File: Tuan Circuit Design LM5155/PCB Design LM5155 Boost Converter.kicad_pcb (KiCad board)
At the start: 4 copper layers, 80.2 x 53 mm, 40 parts, among them Q1 BSC035N04LS G, U1 LM5155_DSSR

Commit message: Fix Update
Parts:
- moved C4 2.06 mm to (131.4, 71.8)
- moved C3 1.27 mm to (130.7, 79.9)
- renumbered Vin1 to VIN, Vout1 to VOUT
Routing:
- net /MOSFET: track 46.0 -> 46.9 mm
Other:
- board size 80.2 x 53 mm -> 80 x 53 mm

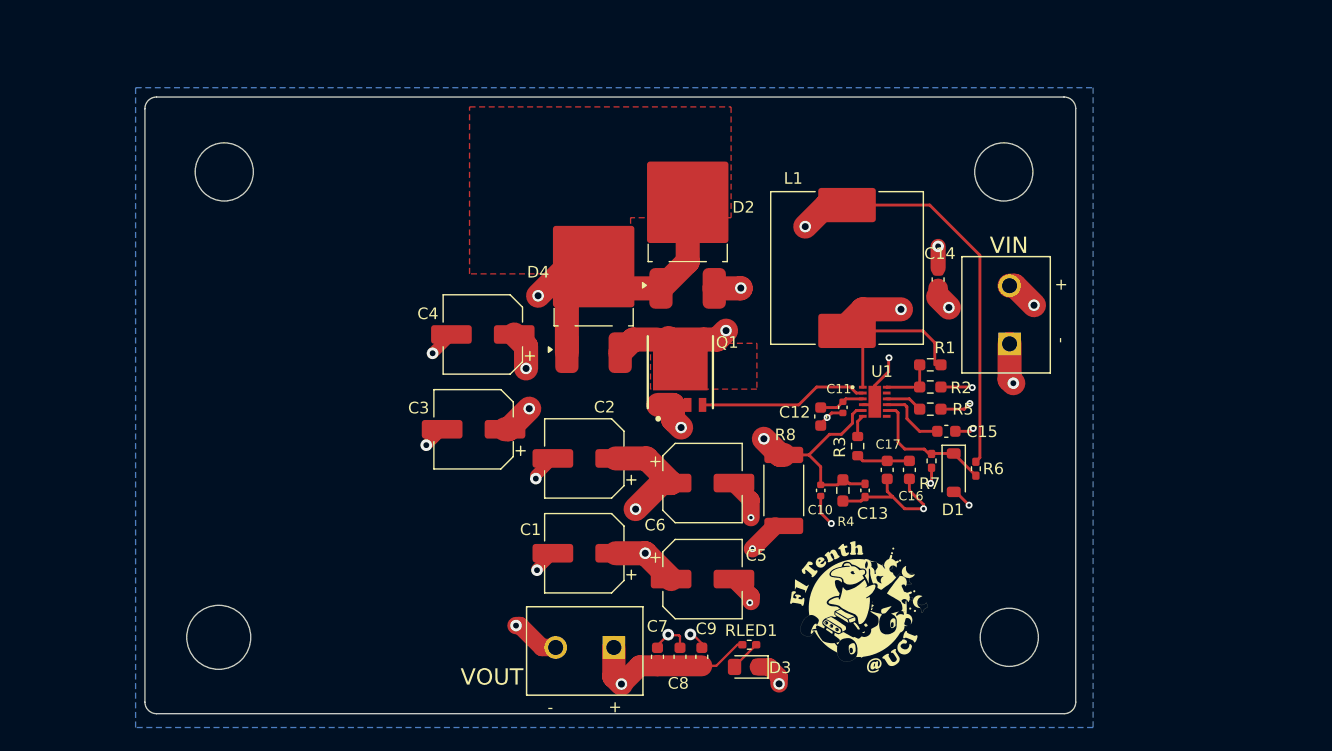
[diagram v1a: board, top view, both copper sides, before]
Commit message: Fix small issue on connection and add resistor
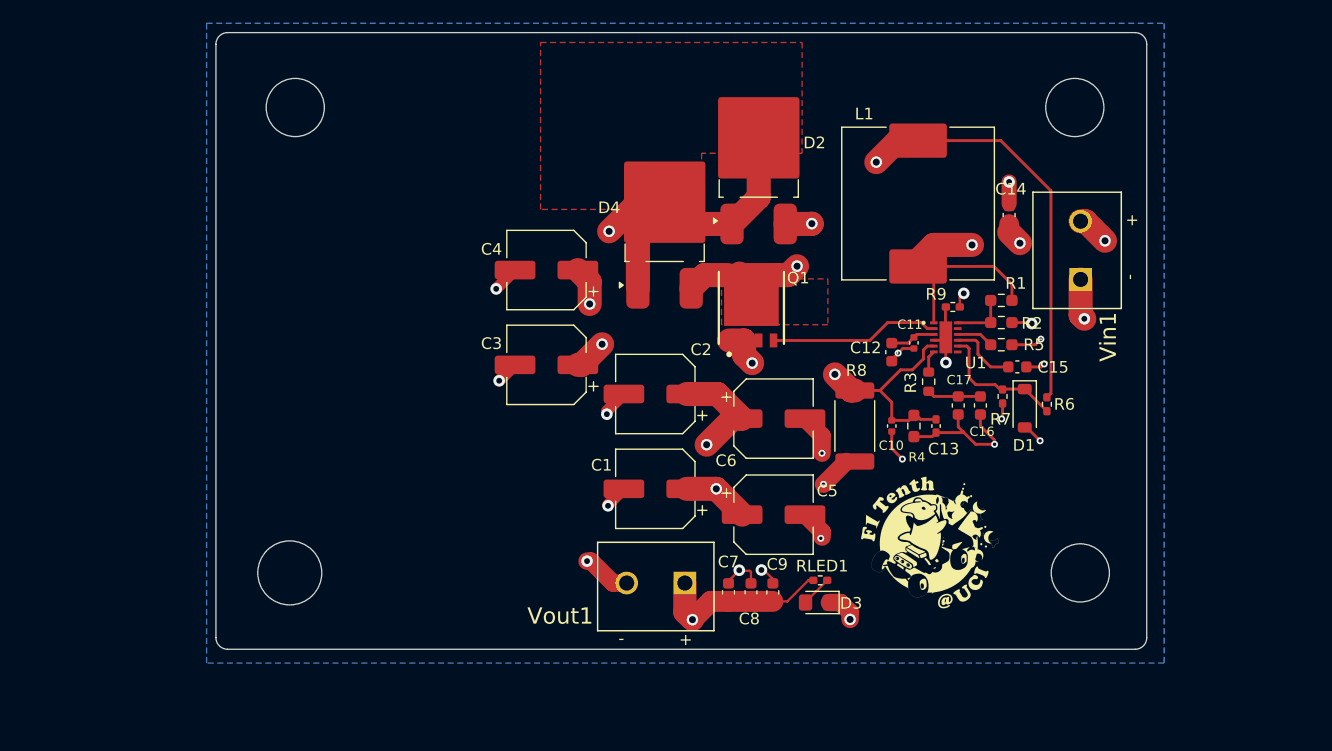
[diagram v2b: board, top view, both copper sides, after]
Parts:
- removed the REF** at (176.7, 97.8)
- removed the REF** at (176.2, 57.8)
- removed the REF** at (109.2, 57.8)
- removed VIN, VOUT: TB002-500-02BE, TB002_500_02BE:CUI_TB002-500-02BE
- added R9: 0, Resistor_SMD:R_0402_1005Metric_Pad0.72x0.64mm_HandSolder, F.Cu at (171.8, 69.4)
- added REF**: MountingHole_5mm, MountingHole:MountingHole_5mm, F.Cu at (182.8, 92.2)
- added REF**: MountingHole_5mm, MountingHole:MountingHole_5mm, F.Cu at (182.3, 52.2)
- added REF**: MountingHole_5mm, MountingHole:MountingHole_5mm, F.Cu at (115.3, 52.2)
- added Vin1: TB002-500-02BE, TB002_500_02BE:CUI_TB002-500-02BE, F.Cu at (182.8, 67.0)
- added Vout1: TB002-500-02BE, TB002_500_02BE:CUI_TB002-500-02BE, F.Cu at (148.8, 93.1)
- moved C3 8.36 mm to (136.9, 74.4)
- moved C12 8.24 mm to (166.6, 73.3)
- moved Q1 8.24 mm to (154.5, 69.5)
- moved U1 8.24 mm to (171.2, 72.0)
- moved C14 8.24 mm to (176.7, 61.5)
- moved D2 8.24 mm to (155.2, 56.9)
- moved C10 8.24 mm to (166.6, 79.6)
- moved C11 8.24 mm to (168.5, 72.5)
- moved C13 8.24 mm to (170.4, 79.6)
- moved C15 8.24 mm to (177.4, 74.5)
- moved C7 8.24 mm to (152.6, 93.9)
- moved C8 8.24 mm to (154.5, 93.9)
- moved C9 8.24 mm to (156.4, 93.9)
- moved D4 8.24 mm to (147.1, 62.4)
- moved R4 8.24 mm to (168.5, 79.6)
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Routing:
- net GNDPWR: track 43.8 -> 44.3 mm
- net GND: track 24.9 -> 25.3 mm, vias 7 -> 8

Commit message: Add switch
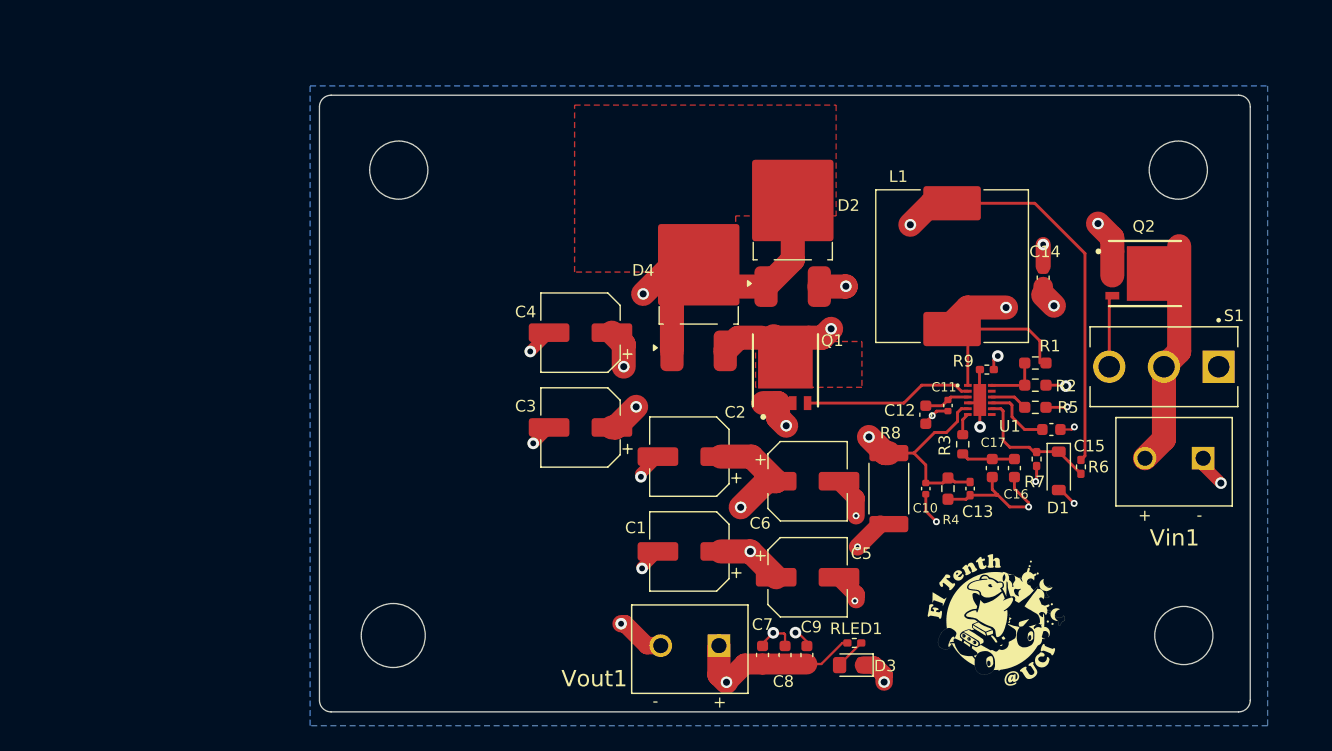
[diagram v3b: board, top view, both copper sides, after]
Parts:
- removed the REF** at (182.8, 92.2)
- removed the REF** at (182.3, 52.2)
- removed the REF** at (115.3, 52.2)
- added Q2: BSC035N04LS G, INF-PG-TDSON-8:INF-PG-TDSON-8, F.Cu at (188.4, 66.5)
- added REF**: MountingHole_5mm, MountingHole:MountingHole_5mm, F.Cu at (124.2, 57.6)
- added REF**: MountingHole_5mm, MountingHole:MountingHole_5mm, F.Cu at (191.2, 57.6)
- added REF**: MountingHole_5mm, MountingHole:MountingHole_5mm, F.Cu at (191.7, 97.6)
- added S1: 100SP1T1B4M2QE, SW_100SP1T1B4M2QE:SW_100SP1T1B4M2QE, F.Cu at (190.0, 74.5)
- moved Vin1 18.6 mm to (193.4, 82.4), turned to 180 degrees
- moved REF** 10.4 mm to (123.7, 97.6)
- moved Ref 8.77 mm to (176.3, 96.4)
- moved C1 6.13 mm to (149.2, 90.4)
- moved C16 6.13 mm to (177.1, 83.2)
- moved C17 6.13 mm to (175.2, 83.2)
- moved C2 6.13 mm to (149.2, 82.3)
- moved C3 6.13 mm to (139.8, 79.7)
- moved C4 6.13 mm to (139.8, 71.6)
- moved C5 6.13 mm to (159.4, 92.6)
- moved C6 6.13 mm to (159.4, 84.4)
- moved D1 6.13 mm to (180.9, 83.5)
- moved D3 6.13 mm to (163.1, 100.2)
- moved R1 6.13 mm to (178.9, 74.2)
- moved R2 6.13 mm to (178.9, 76.1)
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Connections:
- Vin1 pad 2: /INDUCTOR -> Net-(Q2-DRAIN-Pad5)
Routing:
- net Net-(Q2-DRAIN-Pad5): track 0.00 -> 19.4 mm
- net Net-(Q2-GATE): track 0.00 -> 6.21 mm
- net /INDUCTOR: track 26.0 -> 28.0 mm
- net GND: track 25.3 -> 24.1 mm
- net GNDPWR: track 44.3 -> 43.8 mm

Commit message: Update 3D model
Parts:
- removed the REF** at (124.2, 57.6)
- removed the REF** at (191.2, 57.6)
- removed the REF** at (191.7, 97.6)
- added REF**: MountingHole_5mm, MountingHole:MountingHole_5mm, F.Cu at (194.7, 52.8)
- added REF**: MountingHole_5mm, MountingHole:MountingHole_5mm, F.Cu at (195.2, 92.8)
- added REF**: MountingHole_5mm, MountingHole:MountingHole_5mm, F.Cu at (127.7, 52.8)
- moved C4 8.43 mm to (145.3, 65.2), turned to -90 degrees
- moved C3 6.03 mm to (144.3, 75.6), turned to 90 degrees
- moved C15 5.99 mm to (183.8, 75.1)
- moved C7 5.99 mm to (159.0, 94.5)
- moved Q2 5.99 mm to (191.9, 61.7)
- moved R8 5.99 mm to (169.9, 80.2)
- moved Ref 5.99 mm to (179.8, 91.5)
- moved Vin1 5.99 mm to (196.9, 77.5)
- moved C14 5.99 mm to (183.1, 62.0)
- moved D2 5.99 mm to (161.6, 57.4)
- moved L1 5.99 mm to (175.3, 61.0)
- moved REF** 5.99 mm to (127.3, 92.8)
- moved R9 5.99 mm to (178.3, 69.9)
- moved U1 5.99 mm to (177.7, 72.5)
- moved Vout1 5.99 mm to (155.3, 93.7)
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
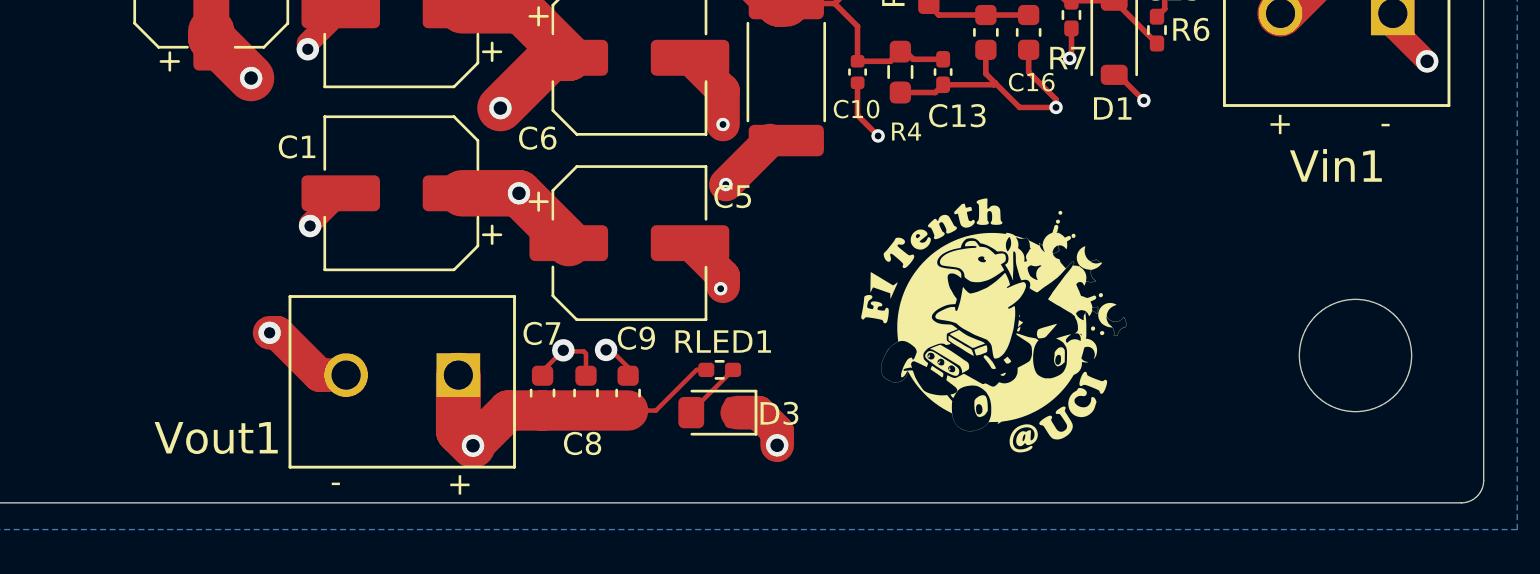
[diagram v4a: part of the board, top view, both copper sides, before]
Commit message: component list purchase
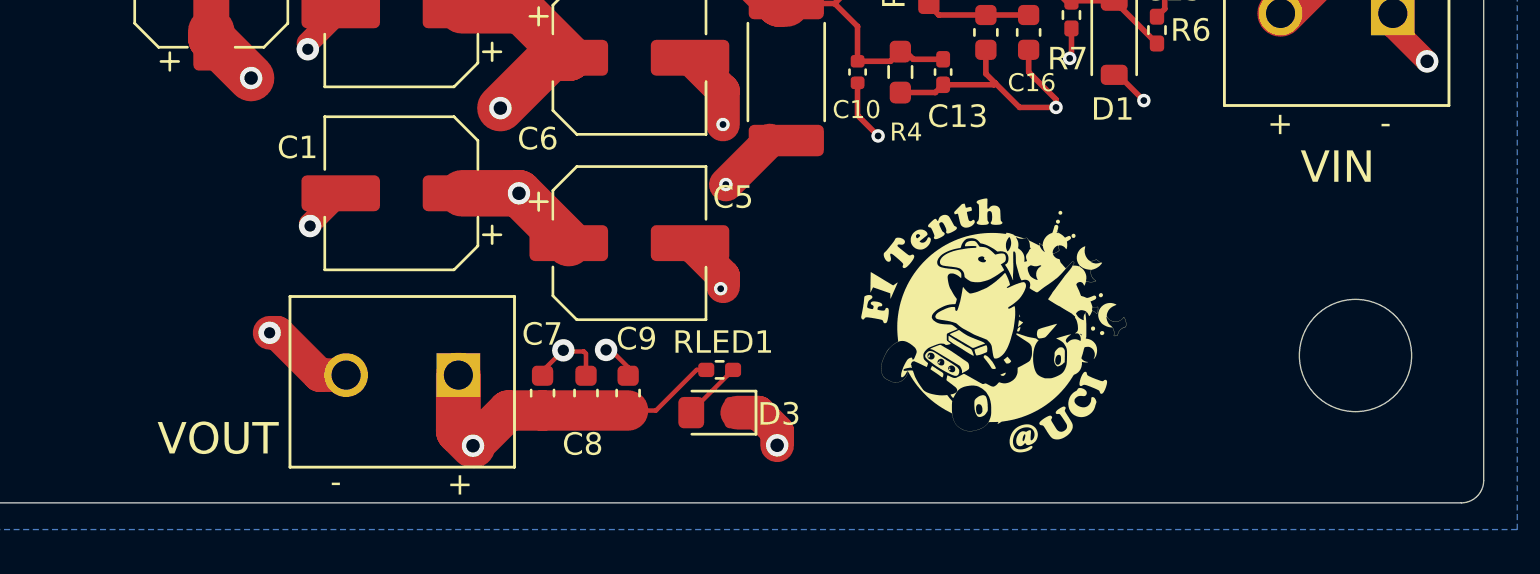
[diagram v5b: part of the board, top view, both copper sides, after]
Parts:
- renumbered Vin1 to VIN, Vout1 to VOUT
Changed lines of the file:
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@@
 		(layer "F.Cu")
 		(at 196.882 77.55 180)
-		(property "Reference" "Vin1"
+		(property "Reference" "VIN"
 			(at 2.455 -6.85 0)
 			(layer "F.SilkS")
@@
 		(layer "F.Cu")
 		(at 155.2624 93.6575 180)
-		(property "Reference" "Vout1"
+		(property "Reference" "VOUT"
 			(at 10.7054 -2.8425 0)
 			(layer "F.SilkS")

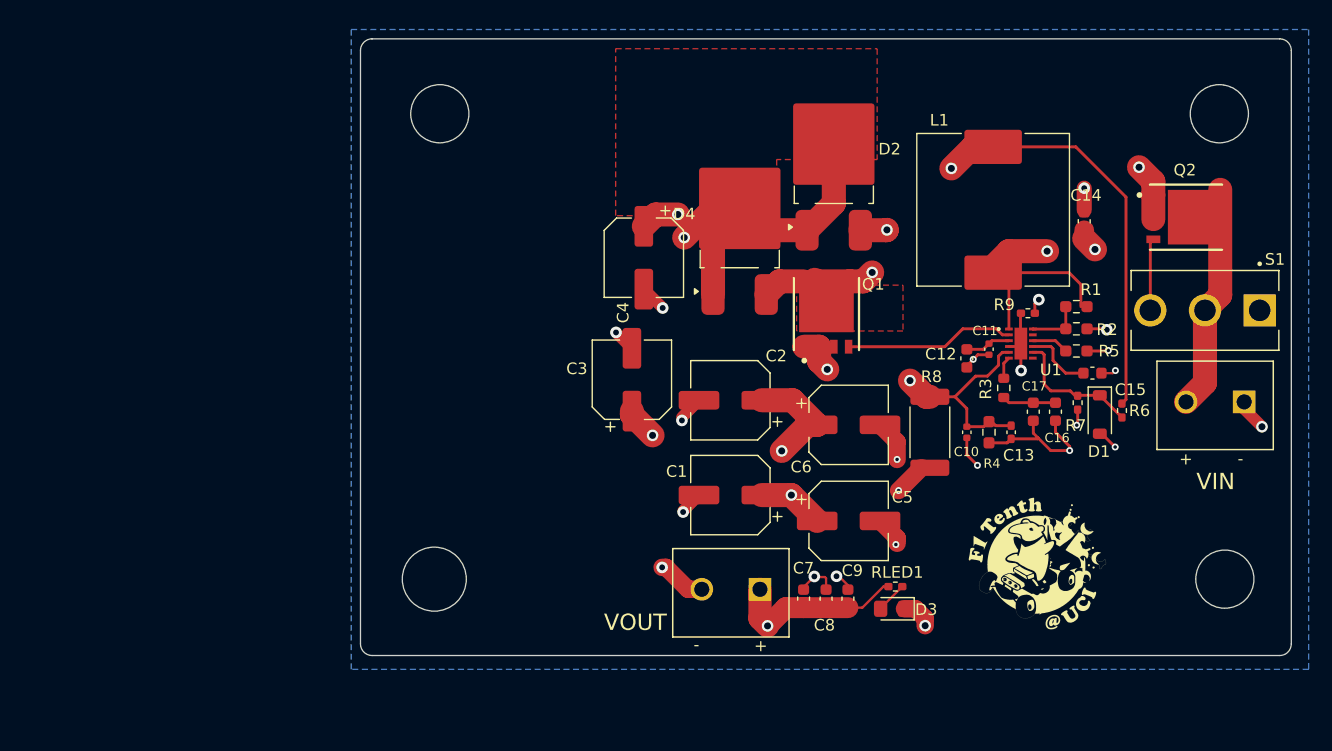
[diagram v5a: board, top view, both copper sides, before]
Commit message: Update voltage protection (TVS and Fuse)
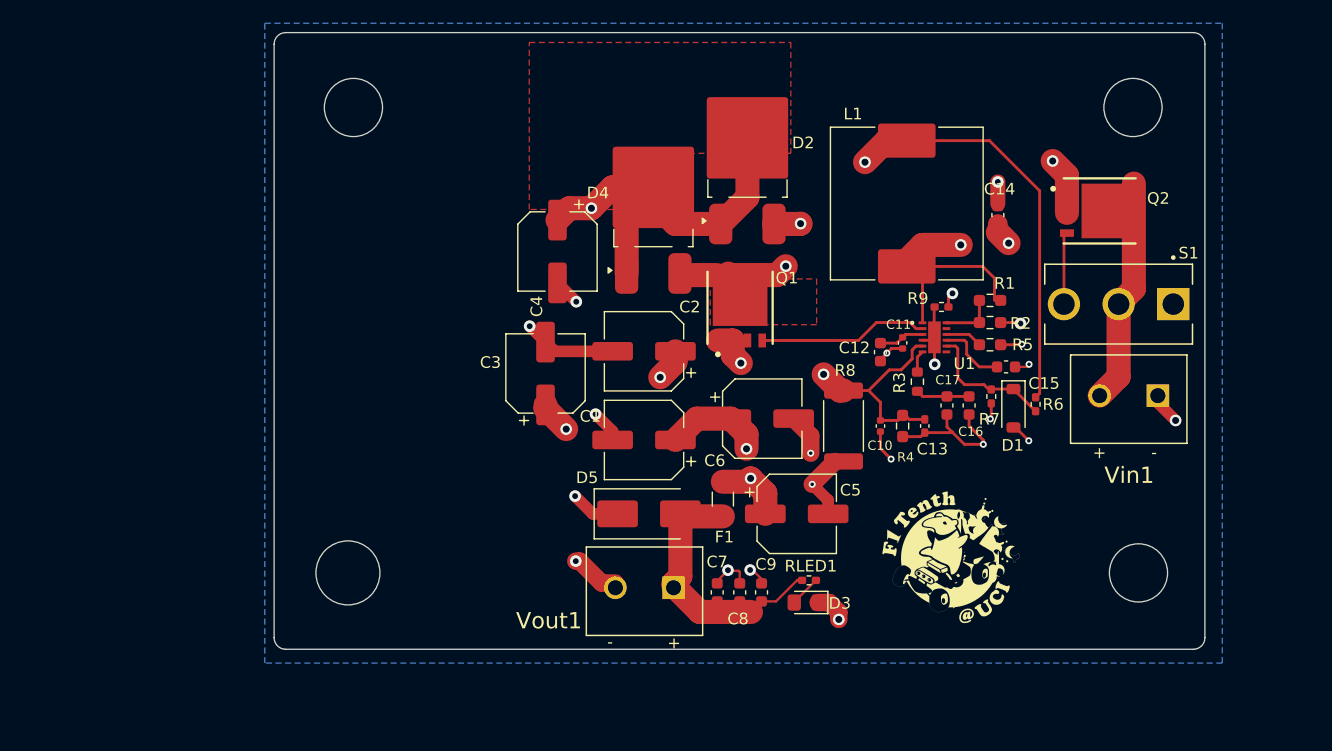
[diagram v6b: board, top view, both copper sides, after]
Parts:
- removed the REF** at (194.7, 52.8)
- removed the REF** at (195.2, 92.8)
- removed the REF** at (127.7, 52.8)
- removed VIN, VOUT: TB002-500-02BE, TB002_500_02BE:CUI_TB002-500-02BE
- added D5: D_TVS, Diode_SMD:D_SMB_Handsoldering, F.Cu at (145.7, 87.2)
- added F1: Fuse, Fuse:Fuse_1206_3216Metric_Pad1.42x1.75mm_HandSolder, F.Cu at (152.1, 85.9)
- added REF**: MountingHole_5mm, MountingHole:MountingHole_5mm, F.Cu at (187.8, 92.2)
- added REF**: MountingHole_5mm, MountingHole:MountingHole_5mm, F.Cu at (120.3, 52.2)
- added REF**: MountingHole_5mm, MountingHole:MountingHole_5mm, F.Cu at (187.3, 52.2)
- added Vin1: TB002-500-02BE, TB002_500_02BE:CUI_TB002-500-02BE, F.Cu at (189.5, 77.0)
- added Vout1: TB002-500-02BE, TB002_500_02BE:CUI_TB002-500-02BE, F.Cu at (147.8, 93.5)
- moved C1 8.81 mm to (145.3, 80.8)
- moved C2 8.53 mm to (145.3, 73.2)
- moved D4 7.64 mm to (146.1, 61.1)
- moved C13 7.44 mm to (169.4, 79.6)
- moved C14 7.44 mm to (175.7, 61.5)
- moved C15 7.44 mm to (176.4, 74.5)
- moved C16 7.44 mm to (173.2, 77.9)
- moved C17 7.44 mm to (171.3, 77.9)
- moved C3 7.44 mm to (136.8, 75.1)
- moved C4 7.44 mm to (137.9, 64.6)
- moved C6 7.44 mm to (155.5, 79.0)
- moved C7 7.44 mm to (151.6, 93.9)
- moved D1 7.44 mm to (177.0, 78.1)
- moved D2 7.44 mm to (154.2, 56.9)
- moved D3 7.44 mm to (159.2, 94.8)
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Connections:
- C7 pad 1: /COUT -> Net-(D5-A2)
- C8 pad 1: /COUT -> Net-(D5-A2)
- C9 pad 1: /COUT -> Net-(D5-A2)
- RLED1 pad 2: /COUT -> Net-(D5-A2)
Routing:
- net Net-(D5-A2): track 0.00 -> 22.0 mm
- net /COUT: track 65.7 -> 55.8 mm, vias 6 -> 5
- net GNDPWR: track 43.8 -> 53.3 mm, vias 15 -> 14
- net /MOSFET: track 46.9 -> 45.3 mm

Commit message: Name Change
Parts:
- renumbered Vin1 to VIN, Vout1 to VOUT
